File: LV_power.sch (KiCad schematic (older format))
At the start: 10 parts, among them J5 BARREL_JACK, U1 V7805-500-SMT, U2 APE8865N-33-HF-3

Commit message: more v2 progress
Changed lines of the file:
@@
 	0    1    1    0
 $EndComp
+$Comp
+L +3.3VA #PWR?
+U 1 1 57F8E4FA
+P 5350 5150
+F 0 "#PWR?" H 5350 5000 50  0001 C CNN
+F 1 "+3.3VA" H 5350 5290 50  0000 C CNN
+F 2 "" H 5350 5150 50  0000 C CNN
+F 3 "" H 5350 5150 50  0000 C CNN
+	1    5350 5150
+	1    0    0    -1
+$EndComp
+$Comp
+L +5VA #PWR?
+U 1 1 57F8E536
+P 4600 5150
+F 0 "#PWR?" H 4600 5000 50  0001 C CNN
+F 1 "+5VA" H 4600 5290 50  0000 C CNN
+F 2 "" H 4600 5150 50  0000 C CNN
+F 3 "" H 4600 5150 50  0000 C CNN
+	1    4600 5150
+	1    0    0    -1
+$EndComp
 $EndSCHEMATC

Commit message: further V2 progress
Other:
- note added: "+3.35VA supply"
- note added: "+3.3VD 400mA supply (POL?)"
- note added: "TVS across +5V rails"
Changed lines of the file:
@@
 	1    0    0    -1
 $EndComp
+Text Notes 3100 1250 0    60   ~ 0
++3.3VD 400mA supply (POL?)
+Text Notes 3100 1350 0    60   ~ 0
++3.35VA supply
+Text Notes 3100 1450 0    60   ~ 0
+TVS across +5V rails
 $EndSCHEMATC

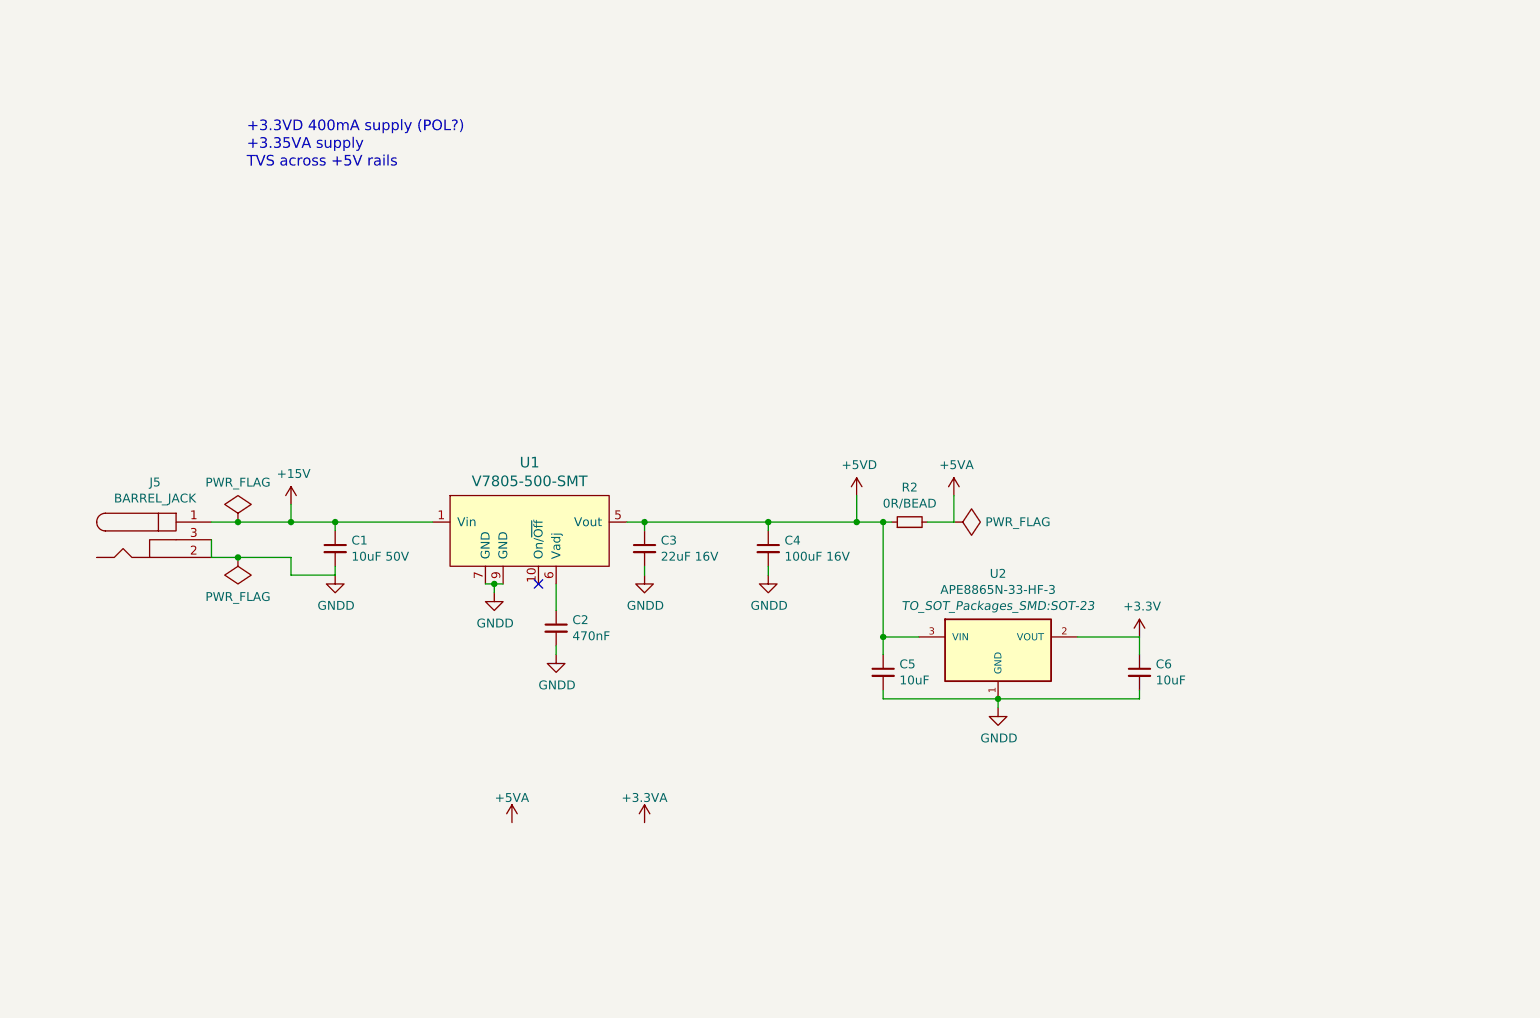
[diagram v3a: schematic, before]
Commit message: V2 schem complete, footprints not assigned
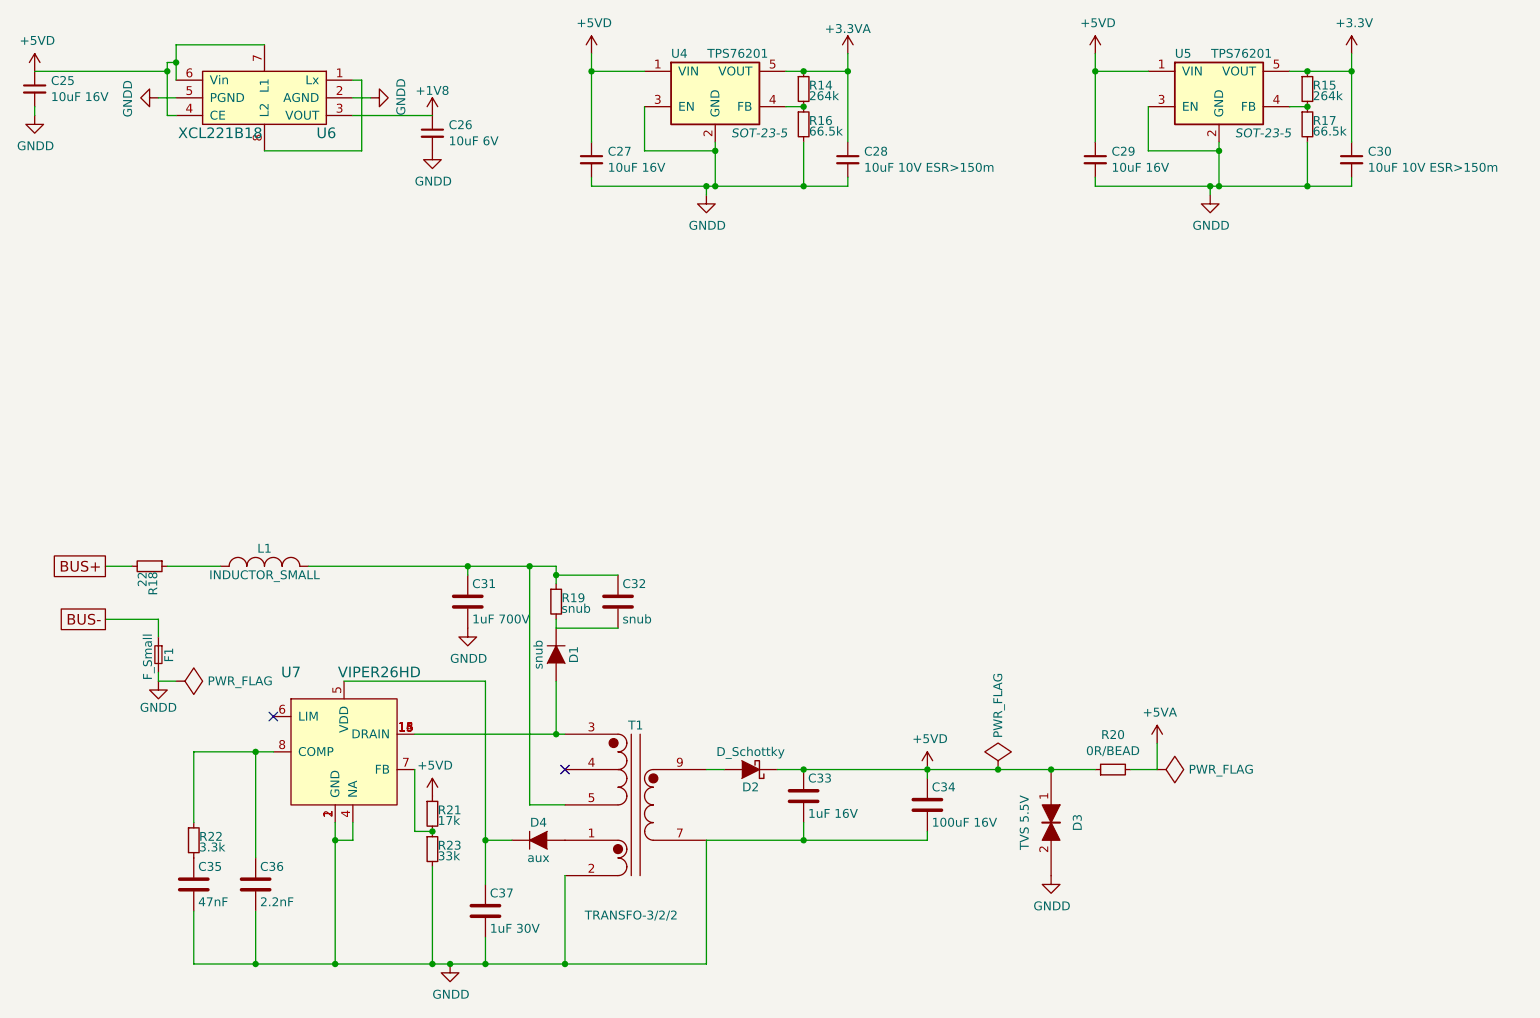
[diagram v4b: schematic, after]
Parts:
- removed C1: 10uF 50V, Capacitors_SMD:C_1210, symbol C_Small
- removed C2: 470nF, Capacitors_SMD:C_0603, symbol C_Small
- removed C3: 22uF 16V, Capacitors_SMD:C_1210, symbol C_Small
- removed C4: 100uF 16V, sictroller:C_6x5, symbol C_Small
- removed J5: BARREL_JACK, sictroller:PJ-102B, symbol BARREL_JACK
- removed U1: V7805-500-SMT, sictroller:V78-500-SMT, symbol V78-500-SMT
- removed U2: APE8865N-33-HF-3, TO_SOT_Packages_SMD:SOT-23, symbol APE8865N-33-HF-3
- added C25: 10uF 16V, Capacitors_SMD:C_0805, symbol C_Small
- added C26: 10uF 6V, Capacitors_SMD:C_0603, symbol C_Small
- added C27: 10uF 16V, Capacitors_SMD:C_1210, symbol C_Small
- added C28: 10uF 10V ESR>150m, Capacitors_SMD:C_1210, symbol C_Small
- added C31: 1uF 700V, symbol C
- added C32: snub, symbol C
- added C33: 1uF 16V, symbol C
- added C34: 100uF 16V, symbol C
- added C35: 47nF, symbol C
- added C36: 2.2nF, symbol C
- added C37: 1uF 30V, symbol C
- added D1: snub, symbol D
- added D2: D_Schottky, symbol D_Schottky
- added D3: TVS 5.5V, symbol TVS
- added D4: aux, symbol D
- added F1: F_Small, symbol F_Small
- added L1: INDUCTOR_SMALL, symbol INDUCTOR_SMALL
- added R14, R15: 264k, symbol R_Small
- added R16, R17: 66.5k, symbol R_Small
- added R18: 22, symbol R_Small
- added R19: snub, symbol R_Small
- added R21: 17k, symbol R_Small
- added R22: 3.3k, symbol R_Small
- added R23: 33k, symbol R_Small
- added T1: TRANSFO-3/2/2, symbol TRANSFO-3/2/2
- added U4, U5: TPS76201, SOT-23-5, symbol TPS76301
- added U6: XCL221B18, symbol XCL221
- added U7: VIPER26HD, symbol VIPER26
- C29: renamed from C5; value 10uF -> 10uF 16V
- C30: renamed from C6; value 10uF -> 10uF 10V ESR>150m
- renumbered R2 to R20
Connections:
- net +3.3VA: now also C28.1, R14.1, U4.5 (VOUT)
- net +3V3: now also R15.1, U5.5 (VOUT)
- net +5VD: now also C25.1, C27.1, C33.1, C34.1, D2.1 (K), D3.1, R21.1, U4.1 (VIN), U5.1 (VIN), U6.4 (CE), U6.6 (Vin), U6.7 (L1)
- net GNDD: now also C25.2, C26.2, C27.2, C28.2, C31.2, C33.2, C34.2, C35.2, C36.2, C37.2, D3.2, F1.2, R16.2, R17.2, R23.2, T1.2 (AUX2), T1.7 (S1), U4.2 (GND), U4.3 (EN), U5.2 (GND), U5.3 (EN), U6.2 (AGND), U6.5 (PGND), U7.1 (GND), U7.2 (GND), U7.4 (NA)
- new net: U6.1 (Lx), U6.8 (L2)
- new net: R15.2, R17.1, U5.4 (FB)
- new net: R14.2, R16.1, U4.4 (FB)
- new net: D1.2 (A), T1.3 (PR1), U7.13 (DRAIN), U7.14 (DRAIN), U7.15 (DRAIN), U7.16 (DRAIN)
- new net: C37.1, D4.1 (K), U7.5 (VDD)
- new net: R21.2, R23.1, U7.7 (FB)
- new net: C36.1, R22.1, U7.8 (COMP)
- new net: D4.2 (A), T1.1 (AUX1)
- new net: C31.1, C32.1, L1.2, R19.1, T1.5 (PR2)
- new net: D2.2 (A), T1.9 (S2)
- new net: C32.2, D1.1 (K), R19.2
- new net: L1.1, R18.1
- new net: C35.1, R22.2
- new net +1V8: C26.1, U6.3 (VOUT)
- new net BUS+: R18.2
- new net BUS-: F1.1
- no-connect marks 1 -> 2
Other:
- note removed: "+3.35VA supply"
- note removed: "+3.3VD 400mA supply (POL?)"
- note removed: "TVS across +5V rails"
- moved on the sheet: C29, C30, R20

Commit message: Add TVS protection to signal I/O.  Reannotate. Assign some footprints.
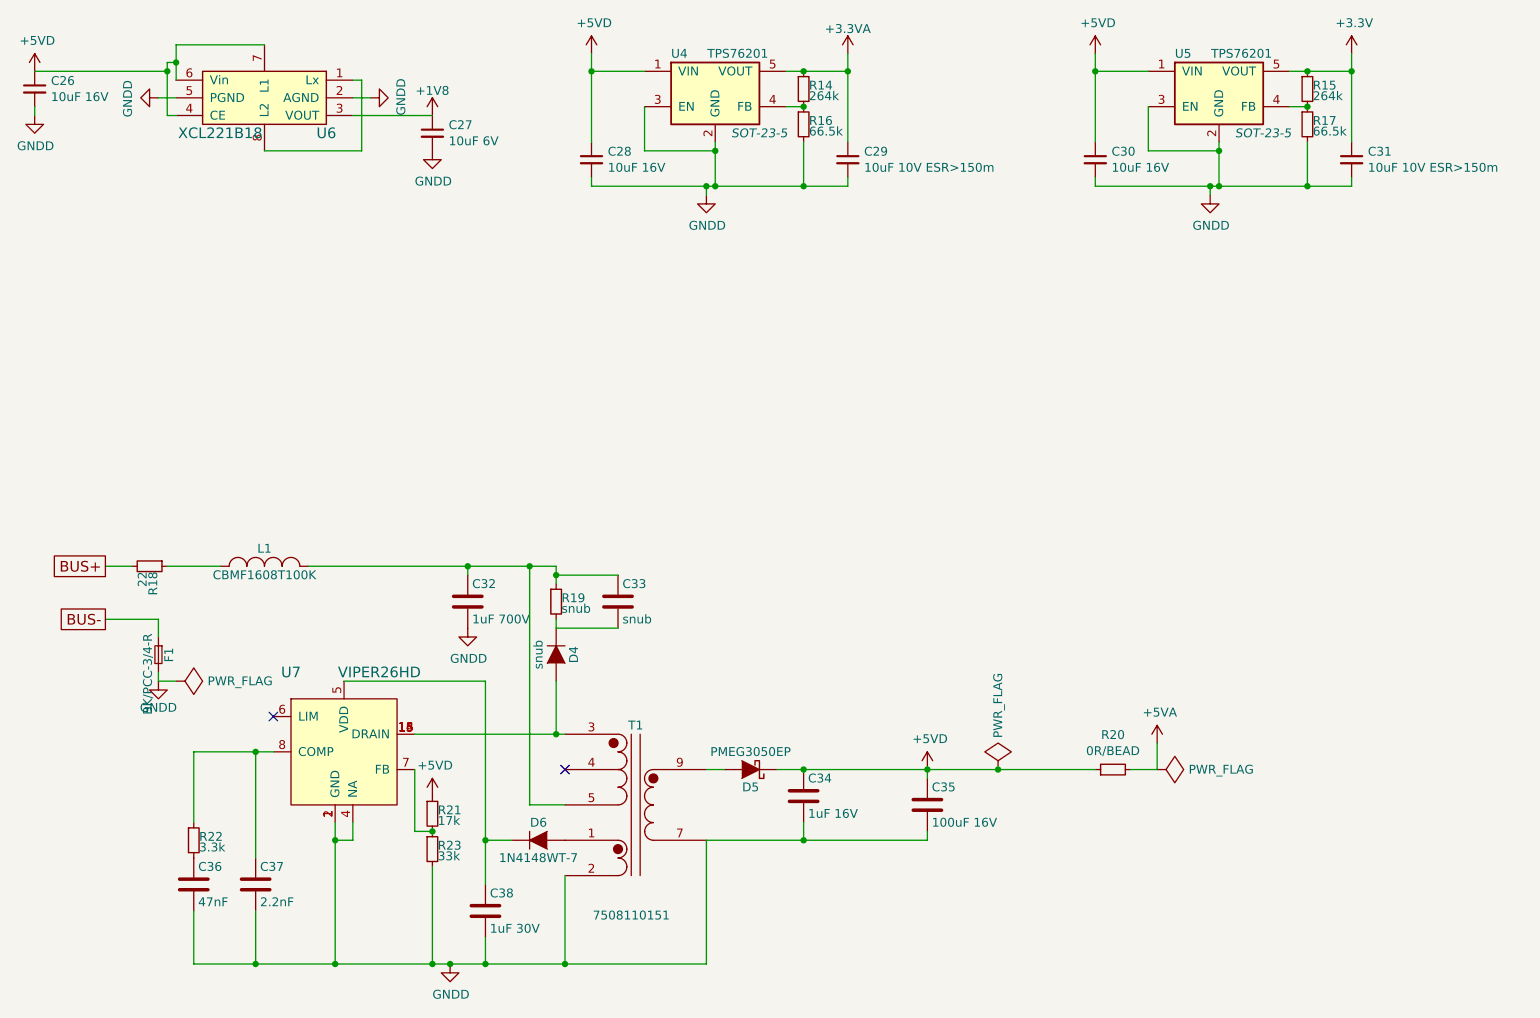
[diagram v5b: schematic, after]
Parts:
- removed D3: TVS 5.5V, symbol TVS
- C28: renamed from C27; footprint Capacitors_SMD:C_1210 -> Capacitors_SMD:C_0805
- C29: renamed from C28; footprint Capacitors_SMD:C_1210 -> Capacitors_SMD:C_0603
- C30: renamed from C29; footprint Capacitors_SMD:C_1210 -> Capacitors_SMD:C_0805
- C31: renamed from C30; footprint Capacitors_SMD:C_1210 -> Capacitors_SMD:C_0603
- C32: renamed from C31; footprint (none) -> sictroller:Ceralink-L
- C34: renamed from C33; footprint (none) -> Capacitors_SMD:C_0603
- C35: renamed from C34; footprint (none) -> sictroller:C_6x5
- C36: renamed from C35; footprint (none) -> Capacitors_SMD:C_0402
- C37: renamed from C36; footprint (none) -> Capacitors_SMD:C_0402
- C38: renamed from C37; footprint (none) -> Capacitors_SMD:C_0603
- D5: renamed from D2; value D_Schottky -> PMEG3050EP; footprint (none) -> sictroller:SOD-128
- D6: renamed from D4; value aux -> 1N4148WT-7; footprint (none) -> Diodes_SMD:SOD-523
- F1: value F_Small -> BK/PCC-3/4-R; footprint (none) -> Fuse_Holders_and_Fuses:Fuse_TE5_Littlefuse-395Series
- L1: value INDUCTOR_SMALL -> CBMF1608T100K; footprint (none) -> Resistors_SMD:R_0603
- R14, R15, R16, R17, R21, R22, R23: footprint (none) -> Resistors_SMD:R_0402
- R18: footprint (none) -> Resistors_SMD:R_0603
- T1: value TRANSFO-3/2/2 -> 7508110151; footprint (none) -> sictroller:WE-7508110151
- U6: footprint (none) -> sictroller:XCL22x
- U7: footprint (none) -> Housings_SOIC:SOIC-16_3.9x9.9mm_Pitch1.27mm
- renumbered C25 to C26, C26 to C27, C32 to C33, D1 to D4

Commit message: footprints assigned for instaspin and LV power
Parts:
- C33: value snub -> 470 pF 800V; footprint (none) -> Capacitors_SMD:C_0805
- D4: value snub -> RS1M; footprint (none) -> Diodes_SMD:SMA_Standard
- R19: value snub -> 100k; footprint (none) -> Resistors_SMD:R_0805
- U4, U5: footprint SOT-23-5 -> TO_SOT_Packages_SMD:SOT-23-5

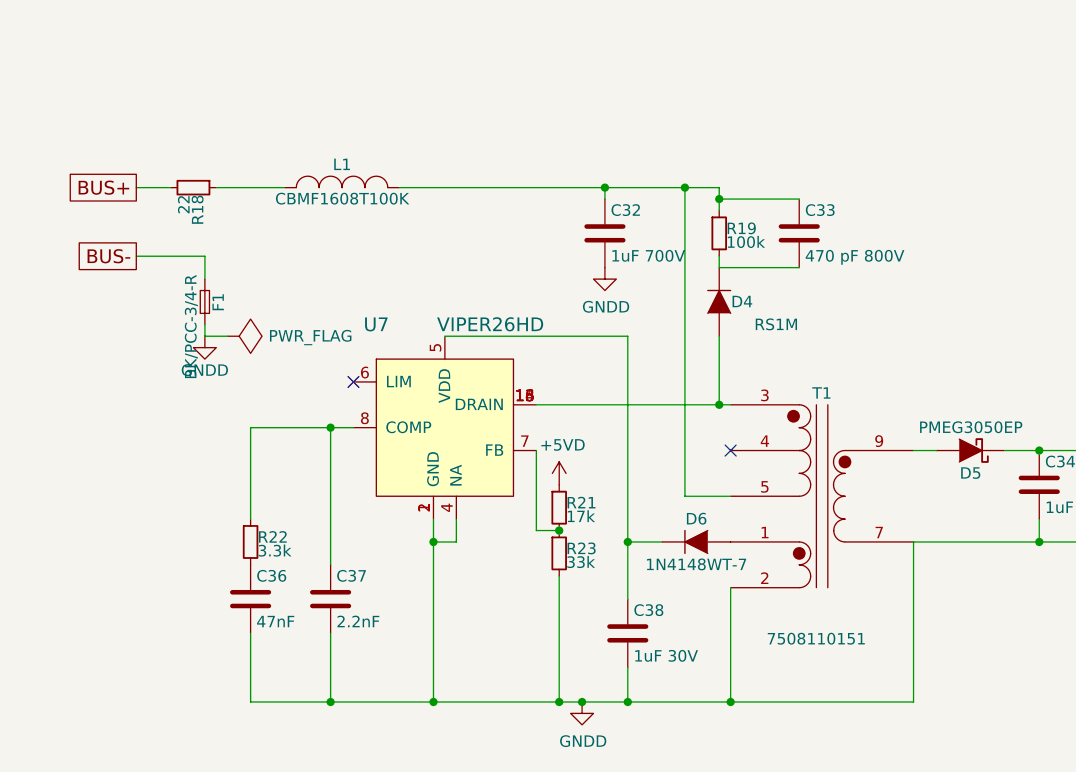
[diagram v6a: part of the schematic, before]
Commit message: started placement of HV-LV stepdown
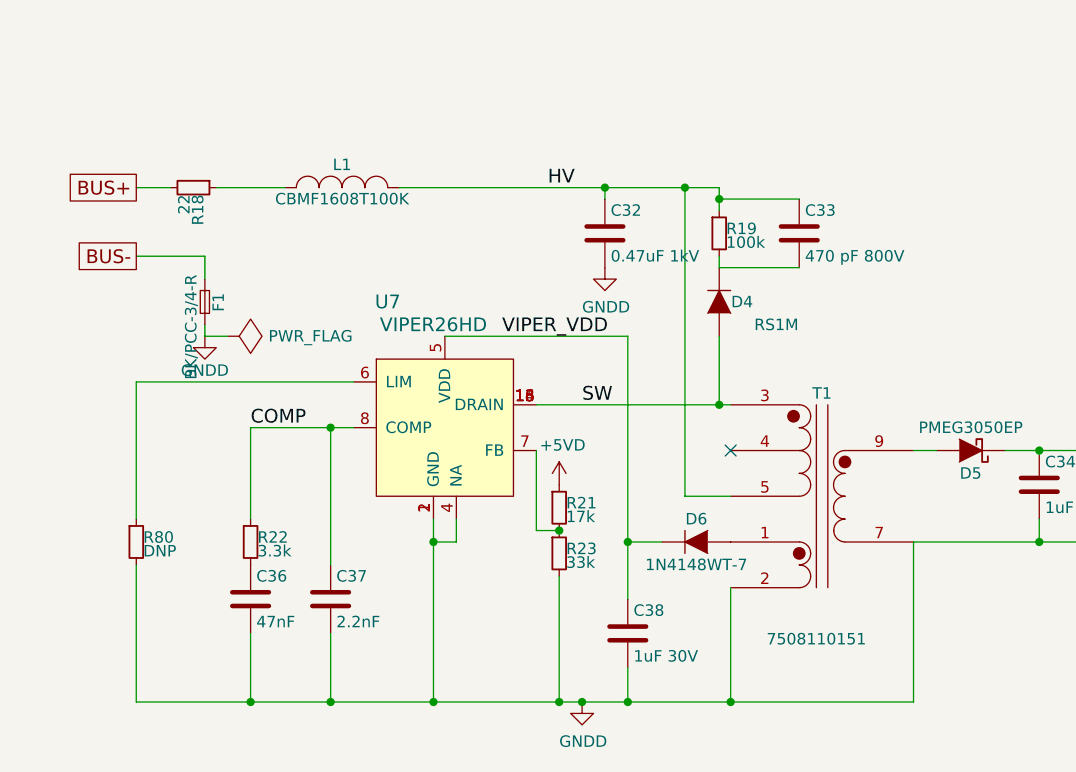
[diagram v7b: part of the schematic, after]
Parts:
- added R80: DNP, Resistors_SMD:R_0402, symbol R_Small
- C32: value 1uF 700V -> 0.47uF 1kV; footprint sictroller:Ceralink-L -> Capacitors_SMD:C_2220
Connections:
- net GNDD: now also R80.2
- net SW: now reaches D4.2 (A), T1.3 (PR1), U7.13 (DRAIN), U7.14 (DRAIN), U7.15 (DRAIN), U7.16 (DRAIN)
- net VIPER_VDD: now reaches C38.1, D6.1 (K), U7.5 (VDD)
- net at U7.6 (LIM): now also R80.1
- net COMP: now reaches C37.1, R22.1, U7.8 (COMP)
- net HV: now reaches C32.1, C33.1, L1.2, R19.1, T1.5 (PR2)
- no-connect marks 2 -> 1
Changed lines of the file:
@@
 U 1 1 57FB521D
 P 3650 4550
-F 0 "U7" H 3350 4800 60  0000 C CNN
-F 1 "VIPER26HD" H 3850 4800 60  0000 C CNN
+F 0 "U7" H 3400 4900 60  0000 C CNN
+F 1 "VIPER26HD" H 3600 4800 60  0000 C CNN
 F 2 "Housings_SOIC:SOIC-16_3.9x9.9mm_Pitch1.27mm" H 3750 4550 60  0001 C CNN
 F 3 "" H 3750 4550 60  0000 C CNN
@@
 P 4350 3900
 F 0 "C32" H 4375 4000 50  0000 L CNN
-F 1 "1uF 700V" H 4375 3800 50  0000 L CNN
-F 2 "sictroller:Ceralink-L" H 4388 3750 50  0001 C CNN
+F 1 "0.47uF 1kV" H 4375 3800 50  0000 L CNN
+F 2 "Capacitors_SMD:C_2220" H 4388 3750 50  0001 C CNN
 F 3 "" H 4350 3900 50  0000 C CNN
 	1    4350 3900
@@
 	0    1    1    0
 $EndComp
-NoConn ~ 3250 4550
 NoConn ~ 4900 4850
 Wire Wire Line
@@
 	3450 3700 4850 3700
 Wire Wire Line
-	2800 5950 5700 5950
+	2300 5950 5700 5950
 Wire Wire Line
 	3600 5150 3600 5950
@@
 Wire Wire Line
 	4850 4350 4850 4650
+Text Label 4250 4650 0    60   ~ 0
+SW
+Text Label 4100 3700 0    60   ~ 0
+HV
+Text Label 3900 4350 0    60   ~ 0
+VIPER_VDD
+Text Label 2800 4750 0    60   ~ 0
+COMP
+$Comp
+L R_Small R80
+U 1 1 5804A7B3
+P 2300 5250
+F 0 "R80" H 2330 5270 50  0000 L CNN
+F 1 "DNP" H 2330 5210 50  0000 L CNN
+F 2 "Resistors_SMD:R_0402" H 2300 5250 50  0001 C CNN
+F 3 "" H 2300 5250 50  0000 C CNN
+	1    2300 5250
+	1    0    0    -1
+$EndComp
+Wire Wire Line
+	2300 5950 2300 5350
+Connection ~ 2800 5950
+Wire Wire Line
+	2300 5150 2300 4550
+Wire Wire Line
+	2300 4550 3250 4550
 $EndSCHEMATC
